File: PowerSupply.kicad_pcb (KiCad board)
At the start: 2 copper layers, 22 x 12.5 mm, 8 parts, among them P1 USB_OTG, P2 CONN_01X03, U1 LM3671MF-3.3

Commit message: Reduced solder mask clearance (1 mil), added fillet corner smoothing to pour areas (0.005 in)
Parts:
- added L1: 4.7uH, 1.2A, PowerSupply:CDRH2D09, F.Cu at (75.6, 152.6)
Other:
- rule pad_to_mask_clearance: 0.2 -> 0.0254
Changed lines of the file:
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@@
 (kicad_pcb (version 4) (host pcbnew 4.0.3-stable)
   (general
-    (links 18)
+    (links 0)
     (no_connects 0)
     (area 49.924999 149.924999 72.075001 162.575001)
@@
     (tracks 62)
     (zones 0)
-    (modules 8)
+    (modules 9)
     (nets 6)
   )
@@
     (pad_size 0.9 0.9)
     (pad_drill 0.9)
-    (pad_to_mask_clearance 0.2)
+    (pad_to_mask_clearance 0.0254)
     (aux_axis_origin 73.205 144.735)
     (visible_elements 7FFCFFFF)
@@
     )
   )
+  (module PowerSupply:CDRH2D09 (layer F.Cu)
+    (at 75.63 152.62 90)
+    (descr "1.3x1.3mm 1.7mm between. Fits Sumida CDRH2D09, CDRH2D18 inductor")
+    (fp_text reference L1 (at 2.8 -0.7 90) (layer F.SilkS)
+      (effects (font (size 0.38608 0.38608) (thickness 0.032512)) (justify right top))
+    )
+    (fp_text value "4.7uH, 1.2A" (at 2.8 1 90) (layer F.SilkS)
+      (effects (font (size 0.38608 0.38608) (thickness 0.032512)) (justify right top))
+    )
+    (fp_line (start -1.2 -0.9) (end -0.6 -1.5) (layer F.SilkS) (width 0.2032))
+    (fp_line (start -0.6 -1.5) (end 0.6 -1.5) (layer F.SilkS) (width 0.2032))
+    (fp_line (start 0.6 -1.5) (end 1.2 -0.9) (layer F.SilkS) (width 0.2032))
+    (fp_line (start -1.2 0.9) (end -0.6783 1.3739) (layer F.SilkS) (width 0.2032))
+    (fp_arc (start 0 0.639099) (end -0.6783 1.3739) (angle -85.420723) (layer F.SilkS) (width 0.2032))
+    (fp_line (start 0.6783 1.3739) (end 1.2 0.9) (layer F.SilkS) (width 0.2032))
+    (fp_line (start -1.5 0.6) (end -0.7071 1.3929) (layer Dwgs.User) (width 0.03))
+    (fp_arc (start 0 0.685799) (end -0.7071 1.3929) (angle -90) (layer Dwgs.User) (width 0.03))
+    (fp_line (start 0.7071 1.3929) (end 1.5 0.6) (layer Dwgs.User) (width 0.03))
+    (fp_line (start 1.5 0.6) (end 1.5 -0.6) (layer Dwgs.User) (width 0.03))
+    (fp_line (start 1.5 -0.6) (end 0.6 -1.5) (layer Dwgs.User) (width 0.03))
+    (fp_line (start 0.6 -1.5) (end -0.6 -1.5) (layer Dwgs.User) (width 0.03))
+    (fp_line (start -0.6 -1.5) (end -1.5 -0.6) (layer Dwgs.User) (width 0.03))
+    (fp_line (start -1.5 -0.6) (end -1.5 0.6) (layer Dwgs.User) (width 0.03))
+    (pad P$1 smd rect (at -1.5 0 180) (size 1.3 1.3) (layers F.Cu F.Paste F.Mask))
+    (pad P$2 smd rect (at 1.5 0 180) (size 1.3 1.3) (layers F.Cu F.Paste F.Mask))
+  )
   (gr_text volium.com (at 61 152) (layer B.SilkS)
     (effects (font (size 1.5 1.5) (thickness 0.2)) (justify mirror))
@@
   (segment (start 61.46 153.87) (end 61.46 153.03) (width 0.254) (layer F.Cu) (net 1))
   (segment (start 60.6802 154.6498) (end 61.46 153.87) (width 0.254) (layer F.Cu) (net 1))
-  (segment (start 69.75 160.4) (end 55.4 160.4) (width 0.254) (layer B.Cu) (net 2) (status 400000))
+  (segment (start 69.75 160.4) (end 55.4 160.4) (width 0.254) (layer B.Cu) (net 2))
   (via (at 52.5 157.5) (size 0.889) (drill 0.508) (layers F.Cu B.Cu) (net 2))
   (segment (start 53.75 157.5) (end 55 157.5) (width 0.254) (layer F.Cu) (net 2))
@@
   (segment (start 64.5 158) (end 66.66986 158) (width 0.254) (layer F.Cu) (net 3))
   (segment (start 66.66986 158) (end 66.68 158.01014) (width 0.254) (layer F.Cu) (net 3))
-  (segment (start 65.82 154.3) (end 65.82 153.605) (width 0.1524) (layer F.Cu) (net 4))
-  (segment (start 65.82 153.605) (end 66.8525 152.5725) (width 0.1524) (layer F.Cu) (net 4))
-  (segment (start 66.8525 152.5725) (end 69.75 152.5725) (width 0.1524) (layer F.Cu) (net 4))
+  (segment (start 66.7 154.3) (end 68.4275 152.5725) (width 0.1524) (layer F.Cu) (net 4))
+  (segment (start 68.4275 152.5725) (end 69.75 152.5725) (width 0.1524) (layer F.Cu) (net 4))
+  (segment (start 65.82 154.3) (end 66.7 154.3) (width 0.1524) (layer F.Cu) (net 4))
   (segment (start 66.68 160.84986) (end 64.49986 160.84986) (width 0.1524) (layer F.Cu) (net 5))
   (segment (start 64.49986 160.84986) (end 64.45 160.8) (width 0.1524) (layer F.Cu) (net 5))
@@
     (connect_pads yes (clearance 0.254))
     (min_thickness 0.254)
-    (fill yes (arc_segments 16) (thermal_gap 0.508) (thermal_bridge_width 0.508))
+    (fill yes (arc_segments 16) (thermal_gap 0.508) (thermal_bridge_width 0.508) (smoothing fillet) (radius 0.127))
     (polygon
       (pts
-        (xy 57 155) (xy 62.4 155) (xy 63 154.675) (xy 64.2 154.675) (xy 64.2 152.475)
-        (xy 60.475 152.475) (xy 60.475 154.2) (xy 57 154.2)
+        (xy 57.3 154.9) (xy 62.4 154.9) (xy 63 154.675) (xy 64.2 154.675) (xy 64.2 152.475)
+        (xy 60.475 152.475) (xy 60.475 154.2) (xy 57.3 154.2)
       )
     )
@@
     (connect_pads yes (clearance 0.254))
     (min_thickness 0.254)
-    (fill yes (arc_segments 16) (thermal_gap 0.508) (thermal_bridge_width 0.508))
+    (fill yes (arc_segments 16) (thermal_gap 0.508) (thermal_bridge_width 0.508) (smoothing fillet) (radius 0.127))
     (polygon
       (pts
         (xy 62.5 155.5) (xy 62.5 162.5) (xy 50 162.5) (xy 50 150) (xy 60 150)
-        (xy 60 153.5) (xy 56.5 153.5) (xy 56.5 157.5) (xy 60 157.5) (xy 60 155.5)
+        (xy 60 153.5) (xy 56.5 153.5) (xy 56.5 157.6) (xy 60 157.6) (xy 60 155.5)
       )
     )
@@
     (connect_pads yes (clearance 0.254))
     (min_thickness 0.254)
-    (fill yes (arc_segments 16) (thermal_gap 0.508) (thermal_bridge_width 0.508))
+    (fill yes (arc_segments 16) (thermal_gap 0.508) (thermal_bridge_width 0.508) (smoothing fillet) (radius 0.127))
     (polygon
       (pts
@@
     (connect_pads yes (clearance 0.254))
     (min_thickness 0.254)
-    (fill yes (arc_segments 16) (thermal_gap 0.508) (thermal_bridge_width 0.508))
+    (fill yes (arc_segments 16) (thermal_gap 0.508) (thermal_bridge_width 0.508) (smoothing fillet) (radius 0.127))
     (polygon
       (pts
-        (xy 65.2 154.7) (xy 67.5 154.7) (xy 68.5 153.6) (xy 71.05 153.6) (xy 71.05 151.5)
-        (xy 65.2 151.5) (xy 65.2 154.675)
+        (xy 65.2 154.7) (xy 66.5 154.7) (xy 68.5 153.6) (xy 71.05 153.6) (xy 71.05 151.5)
+        (xy 68.5 151.5) (xy 66.5 153.9) (xy 65.2 153.9) (xy 65.2 154.675)
       )
     )
@@
     (connect_pads yes (clearance 0.254))
     (min_thickness 0.254)
-    (fill yes (arc_segments 16) (thermal_gap 0.508) (thermal_bridge_width 0.508))
+    (fill yes (arc_segments 16) (thermal_gap 0.508) (thermal_bridge_width 0.508) (smoothing fillet) (radius 0.127))
     (polygon
       (pts

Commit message: Updates orientation of Inductor (L1), and add test point for VCC)
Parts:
- removed the L1 at (75.6, 152.6)
- added REF***: OSHW-Logo_5.7x6mm_Copper, Symbols:OSHW-Logo_5.7x6mm_Copper, B.Cu at (61.0, 156.2)
- added W1: TEST_1P, Pin_Headers:Pin_Header_Straight_1x01, F.Cu at (63.4, 151.8)
- moved L1 0.97 mm to (68.8, 153.5), turned to 0 degrees
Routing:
- net Net-(L1-Pad1): track 4.65 -> 2.05 mm
- net +3V3: track 10.6 -> 12.4 mm
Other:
- rule pad_to_mask_clearance: 0.0254 -> 0.0762

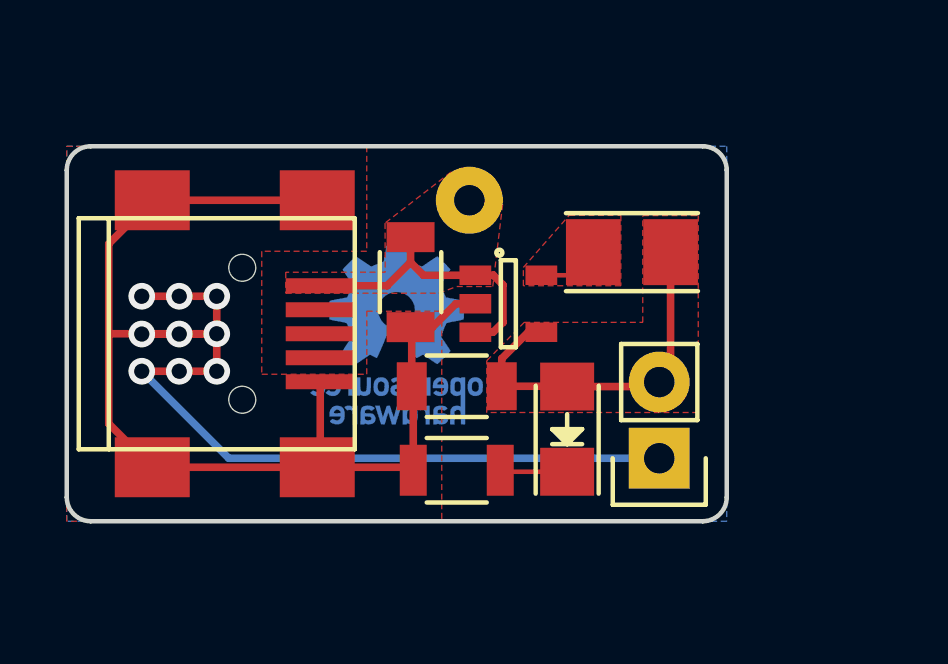
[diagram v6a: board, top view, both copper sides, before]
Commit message: More updates to layout Reduced pad_to_mask clearance, improved solid copper areas, this version also contains OSH (Open Source Hardware) logo, available since previous commit. Added 5V, 3.3V and GND labels to pins. Updated all Gerber files.
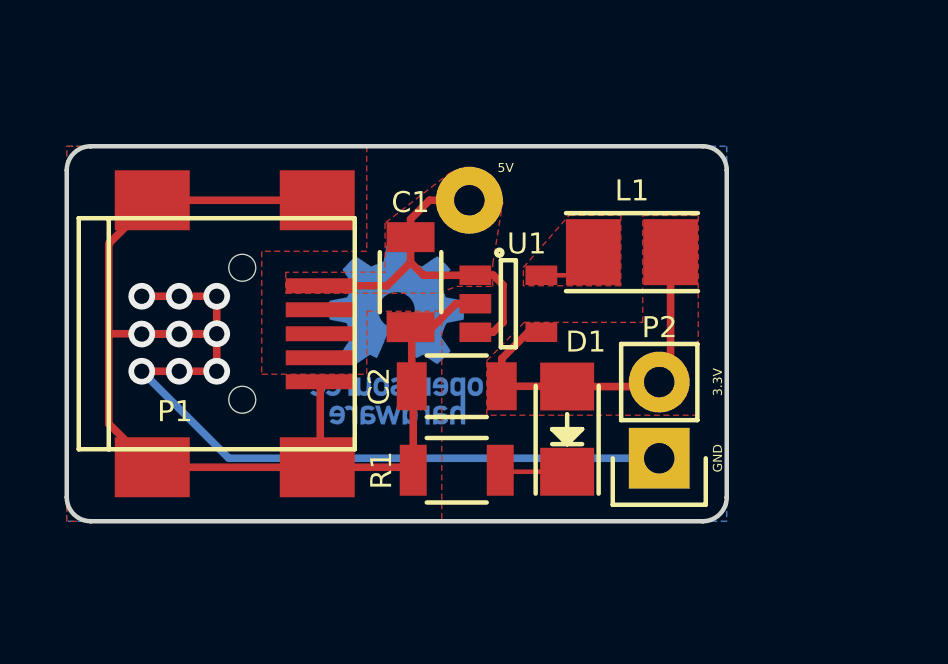
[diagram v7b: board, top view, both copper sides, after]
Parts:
- renumbered W1 to 5V
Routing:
- net VCC: track 9.88 -> 12.7 mm
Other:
- rule pad_to_mask_clearance: 0.0762 -> 0.0508
- board text added: "3.3V"
- board text added: "GND"
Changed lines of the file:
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@@
     (area 49.924999 149.924999 72.075001 162.575001)
     (thickness 1.6)
-    (drawings 10)
-    (tracks 62)
+    (drawings 12)
+    (tracks 65)
     (zones 0)
     (modules 10)
@@
     (pad_size 2.2352 2.2352)
     (pad_drill 1.016)
-    (pad_to_mask_clearance 0.0762)
+    (pad_to_mask_clearance 0.0508)
     (aux_axis_origin 155.36 152.58)
     (grid_origin 155.23 152.45)
-    (visible_elements 7FFCFFFF)
+    (visible_elements 7FFEFFFF)
     (pcbplotparams
       (layerselection 0x010f0_80000001)
@@
     (descr "Through hole pin header")
     (tags "pin header")
-    (fp_text reference W1 (at 0 -5.1) (layer F.SilkS) hide
-      (effects (font (size 1 1) (thickness 0.15)))
+    (fp_text reference 5V (at 1.21 -1.08) (layer F.SilkS)
+      (effects (font (size 0.3 0.3) (thickness 0.05)))
     )
     (fp_text value TEST_1P (at 0 -3.1) (layer F.Fab)
@@
     (tags "inductor taiyo-yuden nr smd")
     (attr smd)
-    (fp_text reference L1 (at -2.99 0.01 90) (layer F.SilkS) hide
-      (effects (font (size 1 1) (thickness 0.15)))
+    (fp_text reference L1 (at 0 -2.05) (layer F.SilkS)
+      (effects (font (size 0.7 0.7) (thickness 0.15)))
     )
     (fp_text value 2.2uH (at 0 2.7) (layer F.Fab)
@@
     (tags "USB USB_B USB_Mini connector")
     (attr smd)
-    (fp_text reference P1 (at -1.07 2.2) (layer F.SilkS) hide
+    (fp_text reference P1 (at -1.39 2.59) (layer F.SilkS)
       (effects (font (size 0.7 0.7) (thickness 0.15)))
     )
@@
     (tags SOT-23-5)
     (attr smd)
-    (fp_text reference U1 (at -0.13 -2.82) (layer F.SilkS) hide
+    (fp_text reference U1 (at 0.61 -2) (layer F.SilkS)
       (effects (font (size 0.7 0.7) (thickness 0.15)))
     )
@@
     (tags "LED1206 SMD")
     (attr smd)
-    (fp_text reference D1 (at 1.45 0 180) (layer F.SilkS) hide
+    (fp_text reference D1 (at 2.91 0.62 180) (layer F.SilkS)
       (effects (font (size 0.7 0.7) (thickness 0.15)))
     )
@@
     (tags "capacitor 1206")
     (attr smd)
-    (fp_text reference C1 (at -3.14 -0.02 360) (layer F.SilkS) hide
-      (effects (font (size 1 1) (thickness 0.15)))
+    (fp_text reference C1 (at -2.66 0 360) (layer F.SilkS)
+      (effects (font (size 0.7 0.7) (thickness 0.15)))
     )
     (fp_text value 10uF (at 0 2.3 270) (layer F.Fab)
@@
     (tags "capacitor 1206")
     (attr smd)
-    (fp_text reference C2 (at 0 0 270) (layer F.SilkS) hide
-      (effects (font (size 1 1) (thickness 0.15)))
+    (fp_text reference C2 (at 2.59 0 270) (layer F.SilkS)
+      (effects (font (size 0.7 0.7) (thickness 0.15)))
     )
     (fp_text value 10uF (at 0 2.3 180) (layer F.Fab)
@@
     (tags "resistor 1206")
     (attr smd)
-    (fp_text reference R1 (at 0 0 270) (layer F.SilkS) hide
-      (effects (font (size 1 1) (thickness 0.15)))
+    (fp_text reference R1 (at 2.51 0 270) (layer F.SilkS)
+      (effects (font (size 0.7 0.7) (thickness 0.15)))
     )
     (fp_text value R (at 0 2.3 180) (layer F.Fab)
@@
     (descr "Through hole pin header")
     (tags "pin header")
-    (fp_text reference P2 (at 2 3.8 270) (layer F.SilkS) hide
-      (effects (font (size 1 1) (thickness 0.15)))
+    (fp_text reference P2 (at -0.01 4.36 180) (layer F.SilkS)
+      (effects (font (size 0.7 0.7) (thickness 0.15)))
     )
     (fp_text value CONN_01X03 (at 0 -3.1 180) (layer F.Fab)
@@
       (xy 0.376964 2.709982)) (layer B.Cu) (width 0.01))
   )
+  (gr_text GND (at 71.7 160.4 90) (layer F.SilkS)
+    (effects (font (size 0.3 0.3) (thickness 0.05)))
+  )
+  (gr_text 3.3V (at 71.7 157.86 90) (layer F.SilkS)
+    (effects (font (size 0.3 0.3) (thickness 0.05)))
+  )
   (gr_text volium.com (at 57.3 160.88) (layer B.SilkS)
     (effects (font (size 1.5 1.5) (thickness 0.2)) (justify mirror))
@@
   (gr_arc (start 50.8 150.8) (end 50 150.8) (angle 90) (layer Edge.Cuts) (width 0.15))
   (gr_arc (start 71.2 161.7) (end 72 161.7) (angle 90) (layer Edge.Cuts) (width 0.15))
+  (segment (start 63.42 151.8) (end 62.09 151.8) (width 0.254) (layer F.Cu) (net 1))
+  (segment (start 61.46 152.43) (end 61.46 153.03) (width 0.254) (layer F.Cu) (net 1))
+  (segment (start 62.09 151.8) (end 61.46 152.43) (width 0.254) (layer F.Cu) (net 1))
   (segment (start 64.54 155.87) (end 64.21 156.2) (width 0.254) (layer F.Cu) (net 1))
   (segment (start 64.21 156.2) (end 63.62 156.2) (width 0.254) (layer F.Cu) (net 1))
@@
     (polygon
       (pts
-        (xy 57.3 154.9) (xy 62.4 154.9) (xy 63 154.675) (xy 64.2 154.675) (xy 64.54 151.85)
-        (xy 62.81 150.86) (xy 60.61 152.56) (xy 60.615 154.2) (xy 57.3 154.2)
+        (xy 57.3 154.9) (xy 62.4 154.9) (xy 63 154.67) (xy 64.2 154.67) (xy 64.2 153.92)
+        (xy 64.54 151.85) (xy 62.81 150.86) (xy 60.61 152.56) (xy 60.615 154.2) (xy 57.3 154.2)
       )
     )
   )
   (zone (net 2) (net_name GND) (layer F.Cu) (hatch edge 0.508)
-    (connect_pads yes (clearance 0.254))
+    (connect_pads yes (clearance 0.381))
     (min_thickness 0.254)
     (fill yes (arc_segments 16) (thermal_gap 0.508) (thermal_bridge_width 0.508) (smoothing fillet) (radius 0.127))
@@
     (polygon
       (pts
-        (xy 65.25 155.87) (xy 69.2 155.87) (xy 69.2 152.31) (xy 71.05 152.31) (xy 71.05 158.875)
-        (xy 64 158.875) (xy 64 157.15)
+        (xy 65.25 155.87) (xy 69.2 155.87) (xy 69.2 152.31) (xy 71.05 152.31) (xy 71.05 158.965)
+        (xy 64 158.965) (xy 64 157.15)
       )
     )
